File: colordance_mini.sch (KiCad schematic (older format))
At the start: 71 parts, among them J1 XLR3, J10 CONN_01X06, J11 CONN_01X04, J12 CONN_01X04, J13 CONN_01X03, J14 CONN_01X03, J15 CONN_01X03, J16 CONN_01X03, J17 CONN_01X04, J2 CONN_01X08, J3 CONN_01X04, J4 CONN_01X03, J5 CONN_01X04, J6 CONN_01X03, J7 CONN_01X04, J8 CONN_01X04, J9 CONN_01X04, SW1 Rotary_Encoder, SW2 Rotary_Encoder, SW3 Rotary_Encoder, SW4 Rotary_Encoder, U1 MAX485CSA+, U2 ROE-0505S, U3 6N137, U4 Teensy3.5

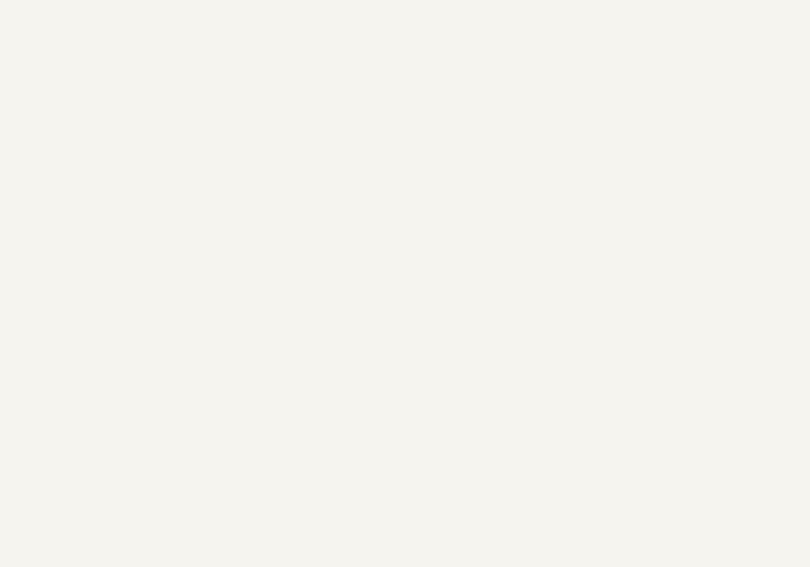
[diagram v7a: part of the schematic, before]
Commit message: Fix holes and generate gerbers
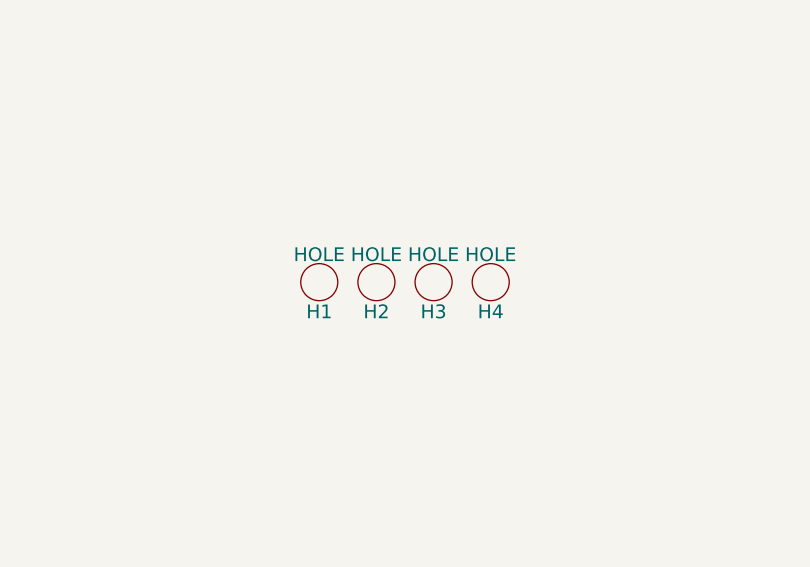
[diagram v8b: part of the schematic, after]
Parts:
- added H1, H2, H3, H4: HOLE, homebrew:HOLE_M4, symbol HOLE
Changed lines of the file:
@@
 Logger
 $Comp
-L GND #PWR053
+L GND #PWR052
 U 1 1 5AC053F0
 P 12450 7500
-F 0 "#PWR053" H 12450 7250 50  0001 C CNN
+F 0 "#PWR052" H 12450 7250 50  0001 C CNN
 F 1 "GND" H 12450 7350 50  0000 C CNN
 F 2 "" H 12450 7500 50  0001 C CNN
@@
 External mic
 $Comp
-L GND #PWR054
+L GND #PWR053
 U 1 1 5ABFBAC6
 P 12450 8300
-F 0 "#PWR054" H 12450 8050 50  0001 C CNN
+F 0 "#PWR053" H 12450 8050 50  0001 C CNN
 F 1 "GND" H 12450 8150 50  0000 C CNN
 F 2 "" H 12450 8300 50  0001 C CNN
@@
 $EndComp
 $Comp
-L +3V3 #PWR055
+L +3V3 #PWR054
 U 1 1 5ABFC360
 P 12450 8100
-F 0 "#PWR055" H 12450 7950 50  0001 C CNN
+F 0 "#PWR054" H 12450 7950 50  0001 C CNN
 F 1 "+3V3" H 12450 8240 50  0000 C CNN
 F 2 "" H 12450 8100 50  0001 C CNN
@@
 SPI
 $Comp
-L GND #PWR056
+L GND #PWR055
 U 1 1 5ABFF1CE
 P 15550 10300
-F 0 "#PWR056" H 15550 10050 50  0001 C CNN
+F 0 "#PWR055" H 15550 10050 50  0001 C CNN
 F 1 "GND" H 15550 10150 50  0000 C CNN
 F 2 "" H 15550 10300 50  0001 C CNN
@@
 Aux connections
 $Comp
-L +3V3 #PWR057
+L +3V3 #PWR056
 U 1 1 5AC00B2E
 P 15550 9800
-F 0 "#PWR057" H 15550 9650 50  0001 C CNN
+F 0 "#PWR056" H 15550 9650 50  0001 C CNN
 F 1 "+3V3" H 15550 9940 50  0000 C CNN
 F 2 "" H 15550 9800 50  0001 C CNN
@@
 $EndComp
 $Comp
-L +3V3 #PWR058
+L +3V3 #PWR057
 U 1 1 5AC041ED
 P 15550 11350
-F 0 "#PWR058" H 15550 11200 50  0001 C CNN
+F 0 "#PWR057" H 15550 11200 50  0001 C CNN
 F 1 "+3V3" H 15550 11490 50  0000 C CNN
 F 2 "" H 15550 11350 50  0001 C CNN
@@
 $EndComp
 $Comp
-L GND #PWR059
+L GND #PWR058
 U 1 1 5AC042F8
 P 15550 11650
-F 0 "#PWR059" H 15550 11400 50  0001 C CNN
+F 0 "#PWR058" H 15550 11400 50  0001 C CNN
 F 1 "GND" H 15550 11500 50  0000 C CNN
 F 2 "" H 15550 11650 50  0001 C CNN
@@
 $EndComp
 $Comp
-L +3V3 #PWR060
+L +3V3 #PWR059
 U 1 1 5AC0539F
 P 15800 11150
-F 0 "#PWR060" H 15800 11000 50  0001 C CNN
+F 0 "#PWR059" H 15800 11000 50  0001 C CNN
 F 1 "+3V3" H 15800 11290 50  0000 C CNN
 F 2 "" H 15800 11150 50  0001 C CNN
@@
 Connection ~ 16500 11550
 $Comp
-L +3V3 #PWR061
+L +3V3 #PWR060
 U 1 1 5AC059D1
 P 16500 11250
-F 0 "#PWR061" H 16500 11100 50  0001 C CNN
+F 0 "#PWR060" H 16500 11100 50  0001 C CNN
 F 1 "+3V3" H 16500 11390 50  0000 C CNN
 F 2 "" H 16500 11250 50  0001 C CNN
@@
 $EndComp
 $Comp
-L +3V3 #PWR062
+L +3V3 #PWR061
 U 1 1 5AC06F8E
 P 15550 12450
-F 0 "#PWR062" H 15550 12300 50  0001 C CNN
+F 0 "#PWR061" H 15550 12300 50  0001 C CNN
 F 1 "+3V3" H 15550 12590 50  0000 C CNN
 F 2 "" H 15550 12450 50  0001 C CNN
@@
 $EndComp
 $Comp
-L GND #PWR063
+L GND #PWR062
 U 1 1 5AC06F94
 P 15550 12750
-F 0 "#PWR063" H 15550 12500 50  0001 C CNN
+F 0 "#PWR062" H 15550 12500 50  0001 C CNN
 F 1 "GND" H 15550 12600 50  0000 C CNN
 F 2 "" H 15550 12750 50  0001 C CNN
@@
 NoConn ~ 21050 4200
 $Comp
-L +5V #PWR064
+L +5V #PWR063
 U 1 1 5AC09D7A
 P 21400 4300
-F 0 "#PWR064" H 21400 4150 50  0001 C CNN
+F 0 "#PWR063" H 21400 4150 50  0001 C CNN
 F 1 "+5V" H 21400 4440 50  0000 C CNN
 F 2 "" H 21400 4300 50  0001 C CNN
@@
 	21400 4300 21050 4300
 $Comp
-L GND #PWR065
+L GND #PWR064
 U 1 1 5AC0A7F4
 P 21200 4400
-F 0 "#PWR065" H 21200 4150 50  0001 C CNN
+F 0 "#PWR064" H 21200 4150 50  0001 C CNN
 F 1 "GND" H 21200 4250 50  0000 C CNN
 F 2 "" H 21200 4400 50  0001 C CNN
@@
 NoConn ~ 21050 4600
 $Comp
-L GND #PWR066
+L GND #PWR065
 U 1 1 5AC0AD40
 P 21200 3500
-F 0 "#PWR066" H 21200 3250 50  0001 C CNN
+F 0 "#PWR065" H 21200 3250 50  0001 C CNN
 F 1 "GND" H 21200 3350 50  0000 C CNN
 F 2 "" H 21200 3500 50  0001 C CNN
@@
 	21050 3500 21050 3400
 $Comp
-L +3V3 #PWR067
+L +3V3 #PWR066
 U 1 1 5AC0B7B4
 P 21550 2100
-F 0 "#PWR067" H 21550 1950 50  0001 C CNN
+F 0 "#PWR066" H 21550 1950 50  0001 C CNN
 F 1 "+3V3" H 21550 2240 50  0000 C CNN
 F 2 "" H 21550 2100 50  0001 C CNN
@@
 	21550 2100 21050 2100
 $Comp
-L +3V3 #PWR068
+L +3V3 #PWR067
 U 1 1 5AC0C171
 P 18200 3500
-F 0 "#PWR068" H 18200 3350 50  0001 C CNN
+F 0 "#PWR067" H 18200 3350 50  0001 C CNN
 F 1 "+3V3" H 18200 3640 50  0000 C CNN
 F 2 "" H 18200 3500 50  0001 C CNN
@@
 $EndComp
 $Comp
-L +3V3 #PWR069
+L +3V3 #PWR068
 U 1 1 5AC0D27D
 P 15550 13500
-F 0 "#PWR069" H 15550 13350 50  0001 C CNN
+F 0 "#PWR068" H 15550 13350 50  0001 C CNN
 F 1 "+3V3" H 15550 13640 50  0000 C CNN
 F 2 "" H 15550 13500 50  0001 C CNN
@@
 $EndComp
 $Comp
-L GND #PWR070
+L GND #PWR069
 U 1 1 5AC0D283
 P 15550 13800
-F 0 "#PWR070" H 15550 13550 50  0001 C CNN
+F 0 "#PWR069" H 15550 13550 50  0001 C CNN
 F 1 "GND" H 15550 13650 50  0000 C CNN
 F 2 "" H 15550 13800 50  0001 C CNN
@@
 NoConn ~ 19050 3800
 $Comp
-L GND #PWR071
+L GND #PWR070
 U 1 1 5AC0DC91
 P 18900 3600
-F 0 "#PWR071" H 18900 3350 50  0001 C CNN
+F 0 "#PWR070" H 18900 3350 50  0001 C CNN
 F 1 "GND" H 18900 3450 50  0000 C CNN
 F 2 "" H 18900 3600 50  0001 C CNN
@@
 $EndComp
 $Comp
-L GND #PWR072
+L GND #PWR071
 U 1 1 5AC140CF
 P 12500 5350
-F 0 "#PWR072" H 12500 5100 50  0001 C CNN
+F 0 "#PWR071" H 12500 5100 50  0001 C CNN
 F 1 "GND" H 12500 5200 50  0000 C CNN
 F 2 "" H 12500 5350 50  0001 C CNN
@@
 	12650 5350 12650 5500
 $Comp
-L +5V #PWR073
+L +5V #PWR072
 U 1 1 5AC14273
 P 13450 5500
-F 0 "#PWR073" H 13450 5350 50  0001 C CNN
+F 0 "#PWR072" H 13450 5350 50  0001 C CNN
 F 1 "+5V" H 13450 5640 50  0000 C CNN
 F 2 "" H 13450 5500 50  0001 C CNN
@@
 	13050 6700 12700 6700
 $Comp
-L GND #PWR074
+L GND #PWR073
 U 1 1 5AC22B68
 P 12800 6700
-F 0 "#PWR074" H 12800 6450 50  0001 C CNN
+F 0 "#PWR073" H 12800 6450 50  0001 C CNN
 F 1 "GND" H 12800 6550 50  0000 C CNN
 F 2 "" H 12800 6700 50  0001 C CNN
@@
 Connection ~ 12800 6700
 $Comp
-L +3V3 #PWR?
+L +3V3 #PWR074
 U 1 1 5AC2FC7B
 P 13350 7400
-F 0 "#PWR?" H 13350 7250 50  0001 C CNN
+F 0 "#PWR074" H 13350 7250 50  0001 C CNN
 F 1 "+3V3" H 13350 7540 50  0000 C CNN
 F 2 "" H 13350 7400 50  0001 C CNN
@@
 	1    0    0    -1
 $EndComp
+$Comp
+L HOLE H1
+U 1 1 5AC34ECC
+P 10450 12050
+F 0 "H1" H 10450 11920 60  0000 C CNN
+F 1 "HOLE" H 10450 12170 60  0000 C CNN
+F 2 "homebrew:HOLE_M4" H 10450 12050 60  0001 C CNN
+F 3 "" H 10450 12050 60  0001 C CNN
+	1    10450 12050
+	1    0    0    -1
+$EndComp
+$Comp
+L HOLE H2
+U 1 1 5AC351B3
+P 10700 12050
+F 0 "H2" H 10700 11920 60  0000 C CNN
+F 1 "HOLE" H 10700 12170 60  0000 C CNN
+F 2 "homebrew:HOLE_M4" H 10700 12050 60  0001 C CNN
+F 3 "" H 10700 12050 60  0001 C CNN
+	1    10700 12050
+	1    0    0    -1
+$EndComp
+$Comp
+L HOLE H3
+U 1 1 5AC352EA
+P 10950 12050
+F 0 "H3" H 10950 11920 60  0000 C CNN
+F 1 "HOLE" H 10950 12170 60  0000 C CNN
+F 2 "homebrew:HOLE_M4" H 10950 12050 60  0001 C CNN
+F 3 "" H 10950 12050 60  0001 C CNN
+	1    10950 12050
+	1    0    0    -1
+$EndComp
+$Comp
+L HOLE H4
+U 1 1 5AC353DE
+P 11200 12050
+F 0 "H4" H 11200 11920 60  0000 C CNN
+F 1 "HOLE" H 11200 12170 60  0000 C CNN
+F 2 "homebrew:HOLE_M4" H 11200 12050 60  0001 C CNN
+F 3 "" H 11200 12050 60  0001 C CNN
+	1    11200 12050
+	1    0    0    -1
+$EndComp
